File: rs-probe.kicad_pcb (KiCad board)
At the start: 4 copper layers, 40 x 14 mm, 108 parts, among them J1 USB_C_Receptacle_USB2.0, J10 Conn_01x01, J11 Conn_01x01, J2 Castellated Vias, J3 Castellated Vias, J4 Castellated Vias, J5 tag-connect-swd, J6 Conn_01x01, J7 Conn_01x01, J8 Conn_01x01, J9 Conn_01x01, Q1 NTZD3155C or CMLDM3757-TR-PBF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, SW1 EVQ-P2002W, T1 Tab, T2 Tab, U1 74LVC1T45GM,115, U10 74LVC1T45GM,115, U11 74LVC1T45GM,115, U12 NCP133AMXADJTCG, U13 NCP133AMXADJTCG, U14 NCP133AMXADJTCG, U2 74LVC1T45GM,115, U3 W25Q8, U4 NUF8401MNT4G, U5 CortexDebug, U6 RP2040, U7 NUF2042XV6T1G, U8 74LVC1T45GM,115, U9 74LVC1T45GM,115, X1 12 MHz

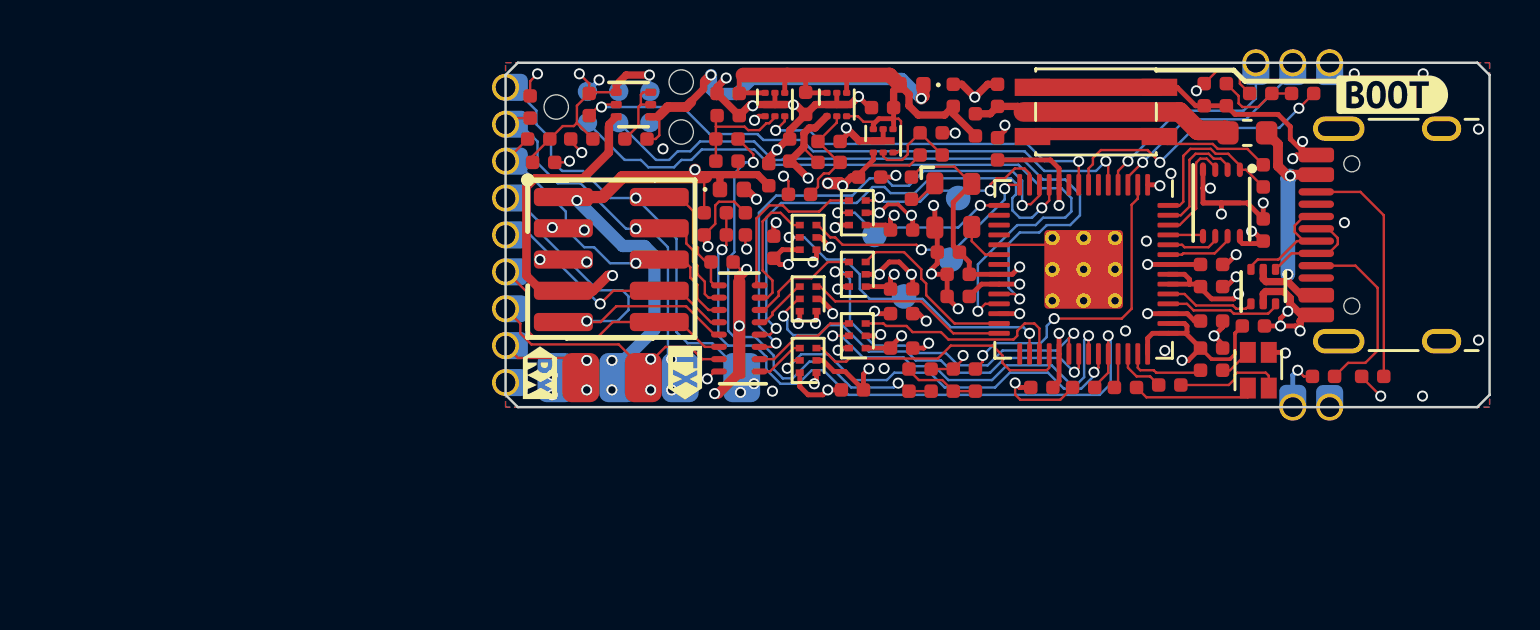
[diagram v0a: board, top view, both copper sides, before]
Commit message: Modification for BillMock-HW on-site programming
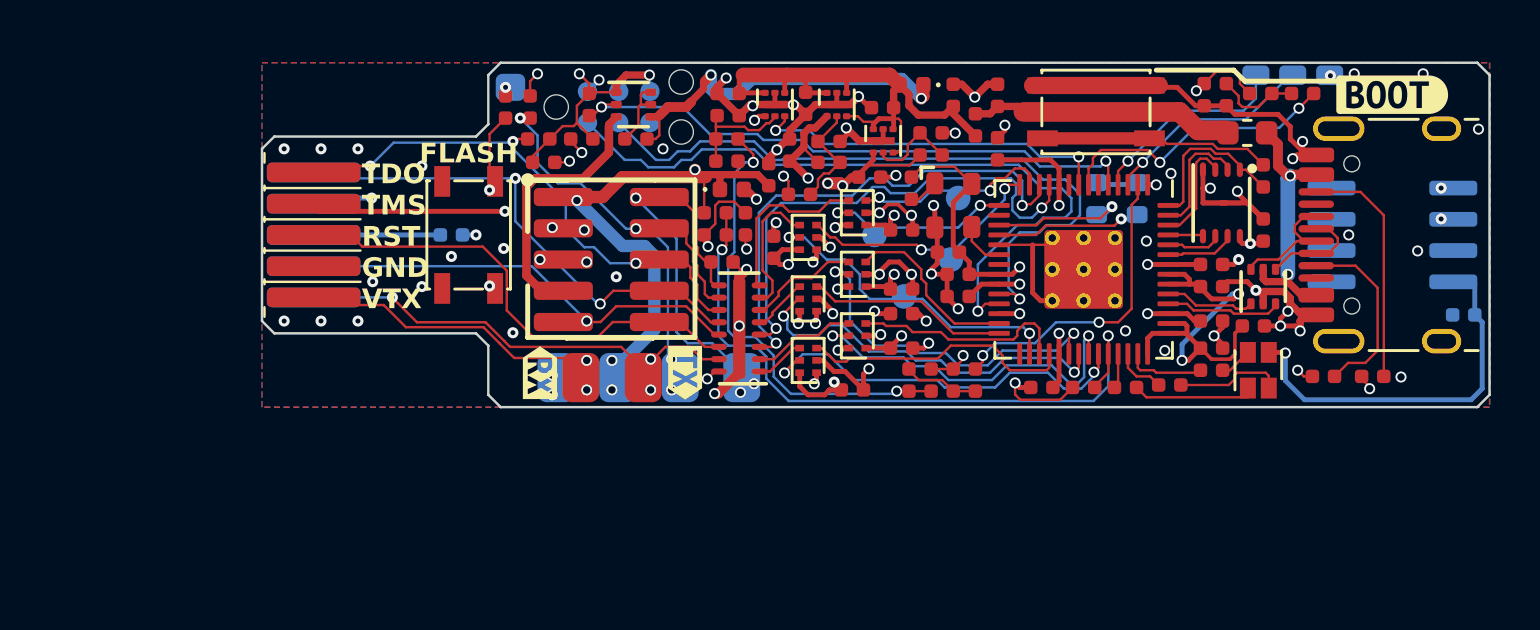
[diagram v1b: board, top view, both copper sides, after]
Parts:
- removed J3: Castellated Vias, connectors:1x2_1.5mm_castellated
- removed kibuzzard-63846A4C: G***, kibuzzard-63846A4C
- removed kibuzzard-6384B72D: G***, kibuzzard-6384B72D
- added C31: 0.1u, passive:C_0402, B.Cu at (187.4, 89.2)
- added J12: Conn_01x01, connectors:pad_1.5x2.0mm, B.Cu at (148.7, 80.0)
- added R30: 0Ω, passive:R_0402, B.Cu at (146.3, 86.0)
- added R31: 1k, passive:R_0402, F.Cu at (148.5, 80.8)
- added R32: 3.3kΩ 1608, passive:R_0603, B.Cu at (172.5, 84.5)
- added R33: 3.3kΩ 1608, passive:R_0603, B.Cu at (174.2, 84.5)
- added SW2: TS-1145A-C-B, Button_Switch_SMD_Extended:SW_SPST_TS-1145A, F.Cu at (147.0, 86.0)
- added SYM1: SYM_Arrow45_Normal, Symbol_Extended:LamudaEE-12.3x7.6mm, B.Cu at (173.3, 89.1)
- added U15: FM24V02A-GTR, Package_SO:SOIC-8_3.9x4.9mm_P1.27mm, B.Cu at (184.6, 86.0)
- J2: value Castellated Vias -> Conn_02x05_Odd_Even; footprint connectors:1x9_1.5mm_castellated -> tc-custom:TC2050-ProbeMod; moved to F.Cu
- Q1: value NTZD3155C or CMLDM3757-TR-PBFREE or DMC2400UV-7 or DMG1016VQ-7 -> NTZD3155C
- SW1: value EVQ-P2002W -> TS-1145A-C-B; footprint Button_Switch_SMD:SW_SPST_EVQP2 -> Button_Switch_SMD_Extended:SW_SPST_TS-1145A
- U1, U10, U11, U2, U8, U9: value 74LVC1T45GM,115 -> 74LVC1T45FZ4-7; footprint Package_TO_SOT_SMD:SOT-886 -> Package_DFN_QFN_Extended:X2-DFN1410-6
- U3: value W25Q8 -> IS25WP016D-JULE-TR
- moved J2 9.84 mm to (140.7, 86.0), turned to 0 degrees
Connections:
- J2 pad 1: GND -> /T_SWO_TDO
- J2 pad 2: /T_VCP_RX -> /T_TDI
- J2 pad 3: /T_VCP_TX -> /T_SWDIO_TMS
- J2 pad 4: /T_~{RESET} -> /T_SWDCLK_JCLK
- J2 pad 5: /T_TDI -> /T_~{RESET}
- J2 pad 6: /T_GNDDetect -> /T_VCC_PROTECT
- J2 pad 7: /T_SWO_TDO -> GND
- J2 pad 8: /T_SWDCLK_JCLK -> /T_GNDDetect
- J2 pad 9: /T_SWDIO_TMS -> /T_VCP_RX
- U6 pad 17: unconnected-(U6-GPIO14-Pad17) -> /FRAM_SDA
- U6 pad 18: unconnected-(U6-GPIO15-Pad18) -> /FRAM_SCL
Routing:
- net /5V_KEY: track 51.8 -> 10.9 mm, vias 3 -> 0
- net /GPIO1: track 8.87 -> 39.0 mm, vias 1 -> 2
- net +3.3V: track 58.5 -> 81.0 mm
- net /FRAM_SDA: track 0.00 -> 19.4 mm, vias 0 -> 2
- net /FRAM_SCL: track 0.00 -> 19.0 mm, vias 0 -> 2
- net /T_SWDCLK_JCLK: track 21.1 -> 30.8 mm, vias 3 -> 5
- net /T_TDI: track 15.3 -> 24.8 mm, vias 2 -> 3
- net /T_SWO_TDO: track 13.4 -> 22.6 mm, vias 1 -> 3
- net /T_VCP_RX: track 22.0 -> 30.2 mm
- net /T_~{RESET}: track 10.9 -> 19.1 mm
- net /T_VCP_TX: track 17.3 -> 24.7 mm, vias 3 -> 4
- net Net-(R31-Pad2): track 0.00 -> 7.09 mm, vias 0 -> 2
- net /T_SWDIO_TMS: track 23.6 -> 29.3 mm, vias 3 -> 4
- net /T_VCC: track 50.3 -> 55.8 mm, vias 4 -> 6
- net /T_VCC_PROTECT: track 0.00 -> 5.25 mm
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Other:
- board size 40 x 14 mm -> 49.9 x 14 mm
- board text added: "20240126"
- board text added: "CLK"
- board text added: "FLASH"
- board text added: "FRAM"
- board text added: "GND"
- board text added: "GNDdet"
- board text added: "Lambda Mod - SelfJig"
- board text added: "RST"
- board text added: "Rusty-Probe"
- board text added: "TDI"
- board text added: "TDO"
- board text added: "TMS"
- board text added: "VCC"
- board text added: "VRX"
- board text added: "VTX"
- board text removed: "By Emil Fresk @korken89"
- board text removed: "git: {GITHASH}"

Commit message: Fabricated on JLCPCB (not tested yet)
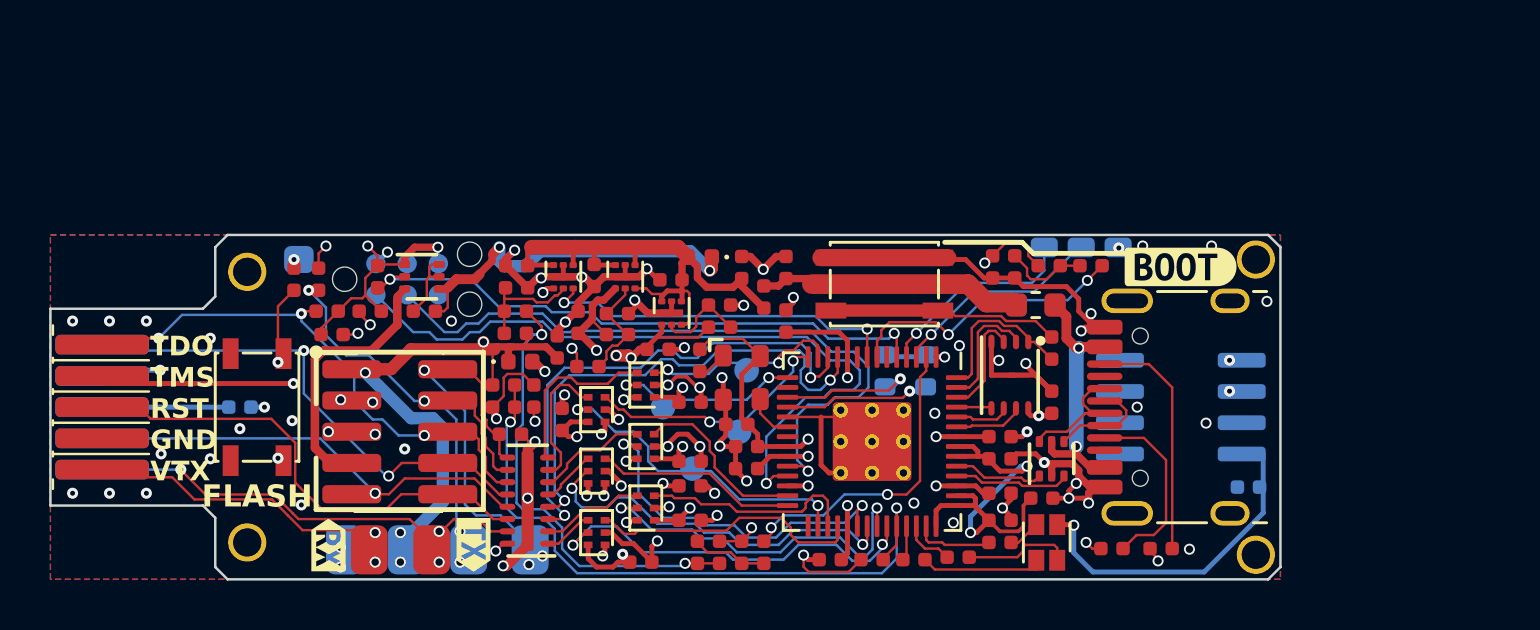
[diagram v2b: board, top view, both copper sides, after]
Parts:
- added T1: Tab, kikit:Tab, F.Cu at (2.90, 1.15)
- added T2: Tab, kikit:Tab, F.Cu at (2.90, 4.45)
- added TH1: MountingHole_2.2mm_M2_DIN965_Pad_TopOnly, MountingHole:MountingHole_2.2mm_M2_DIN965_Pad_TopOnly, F.Cu at (138.0, 87.5)
- added TH2: MountingHole_2.2mm_M2_DIN965_Pad_TopOnly, MountingHole:MountingHole_2.2mm_M2_DIN965_Pad_TopOnly, F.Cu at (179.0, 87.0)
- added TH3: Tooling Hole, , F.Cu at (138.0, 98.5)
- added TH4: Tooling Hole, , F.Cu at (179.0, 99.0)
- moved T1 44.3 mm to (130.0, 93.0), turned to 0 degrees
- moved C31 11.2 mm to (178.7, 96.2)
- moved C14 11.1 mm to (170.7, 92.8)
- moved C21 11.1 mm to (151.4, 89.5)
- moved C23 11.1 mm to (169.2, 87.3)
- moved C25 11.1 mm to (154.7, 90.7)
- moved C3 11.1 mm to (161.7, 99.2)
- moved C8 11.1 mm to (157.2, 98.9)
- moved J6 11.1 mm to (141.9, 98.8)
- moved R18 11.1 mm to (141.4, 90.0)
- moved R2 11.1 mm to (170.7, 90.6)
- moved R20 11.1 mm to (145.2, 89.1)
- moved R22 11.1 mm to (148.7, 94.1)
- moved R30 11.1 mm to (137.7, 93.0)
- moved R33 11.1 mm to (165.6, 91.5)
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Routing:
- net +3.3V: track 81.0 -> 79.4 mm
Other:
- board size 49.9 x 14 mm -> 50 x 14 mm
- board text added: "20240227"
- board text removed: "20240126"
